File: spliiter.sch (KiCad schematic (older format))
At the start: 74 parts, among them U1 NE5532, U2 NE5532, U3 NE5532, U4 NE5532, U5 NE5532

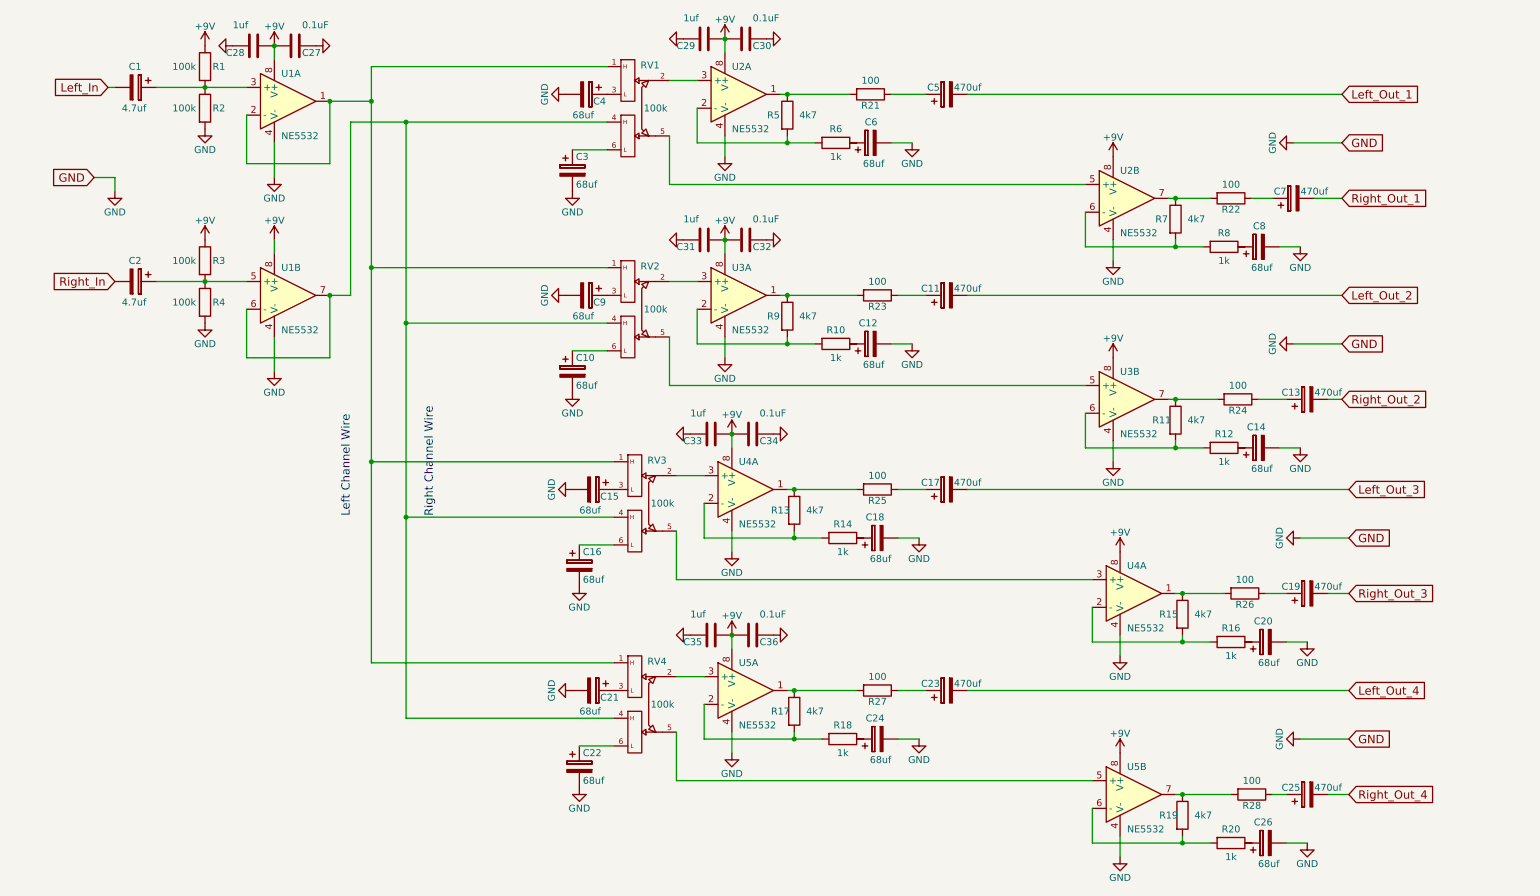
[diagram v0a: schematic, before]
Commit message: Replace +9V to VCC. Electrical rules checker passed
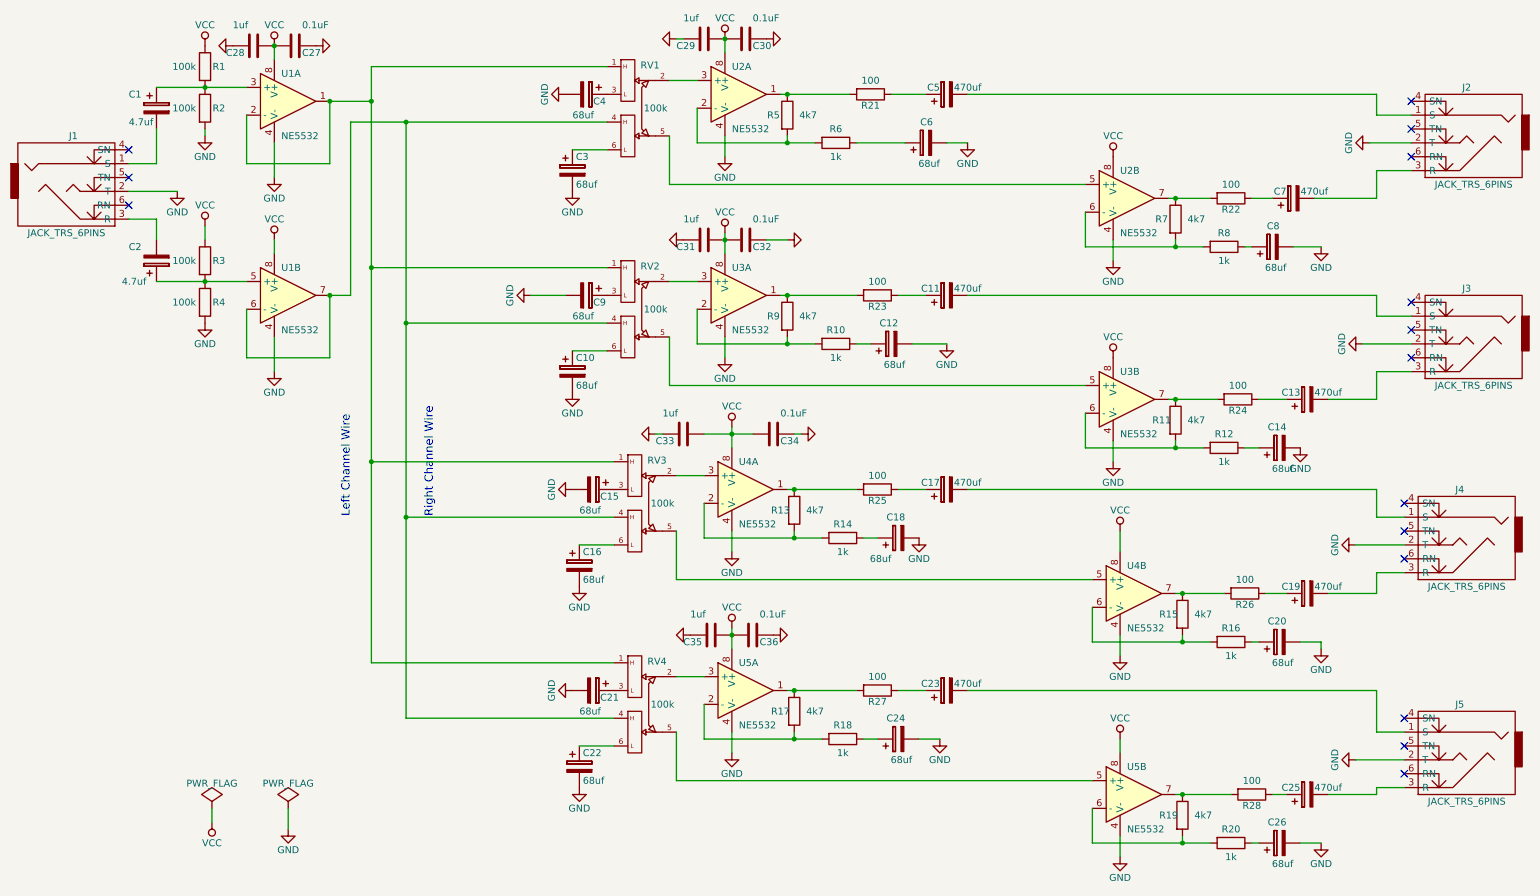
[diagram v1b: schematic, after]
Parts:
- removed U4: NE5532, symbol NE5532
- added J1, J2, J3, J4, J5: JACK_TRS_6PINS, symbol JACK_TRS_6PINS
- added unit 2 of U4
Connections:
- net GND: now also J1.2 (T), J2.2 (T), J3.2 (T), J4.2 (T), J5.2 (T), U4.4 (V-)
- net at R6.1: now also C6.1
- net at R8.1: now also C8.1
- net at R10.1: now also C12.1
- net at R12.1: now also C14.1
- net at RV3.5: now also U4.5 (+)
- net at R14.1: now also C18.1
- net at R15.1, R26.2: now also U4.7
- net at R15.2, R16.2: now also U4.6 (-)
- net at R16.1: now also C20.1
- net at R18.1: now also C24.1
- net at R20.1: now also C26.1
- net +9V renamed VCC
- net VCC: now also U4.8 (V+)
- net Left_In: no longer names the net of C1.2
- net Left_In: now also J1.1 (S)
- net Left_Out_1: no longer names the net of C5.2
- net Left_Out_1: now also J2.1 (S)
- net Left_Out_2: no longer names the net of C11.2
- net Left_Out_2: now also J3.1 (S)
- net Left_Out_3: no longer names the net of C17.2
- net Left_Out_3: now also J4.1 (S)
- net Left_Out_4: no longer names the net of C23.2
- net Left_Out_4: now also J5.1 (S)
- net Right_In: no longer names the net of C2.2
- net Right_In: now also J1.3 (R)
- net Right_Out_1: no longer names the net of C7.2
- net Right_Out_1: now also J2.3 (R)
- net Right_Out_2: no longer names the net of C13.2
- net Right_Out_2: now also J3.3 (R)
- net Right_Out_3: no longer names the net of C19.2
- net Right_Out_3: now also J4.3 (R)
- net Right_Out_4: no longer names the net of C25.2
- net Right_Out_4: now also J5.3 (R)
- no-connect marks 0 -> 15
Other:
- moved on the sheet: C1, C12, C14, C18, C2, C20, C24, C26, C33, C34, C6, C8

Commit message: add some values to netlist
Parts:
- C27, C28, C29, C30, C31, C32, C33, C34, C35, C36: footprint (none) -> Capacitors_SMD:C_0805_HandSoldering
- J1, J2, J3, J4, J5, RV1: footprint (none) -> Connect:PINHEAD1-3
- R1, R10, R11, R12, R13, R14, R15, R16, R17, R18, R19, R2, R20, R21, R22, R23, R24, R25, R26, R27, R28, R3, R4, R5, R6, R7, R8, R9: footprint (none) -> Resistors_SMD:R_0805_HandSoldering
- RV2, RV3, RV4: footprint (none) -> Connect:PINHEAD1-2
- U1, U2, U3, U4, U5: footprint (none) -> Housings_SOIC:SOIC-8_3.9x4.9mm_Pitch1.27mm

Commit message: fix pinheaders
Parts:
- RV2, RV3, RV4: footprint Connect:PINHEAD1-2 -> Connect:PINHEAD1-3
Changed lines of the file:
@@
 F 0 "RV2" H 4710 3010 50  0000 C CNN
 F 1 "100k" H 4750 2700 50  0000 C CNN
-F 2 "Connect:PINHEAD1-2" H 4550 2700 50  0001 C CNN
+F 2 "Connect:PINHEAD1-3" H 4550 2700 50  0001 C CNN
 F 3 "" H 4550 2700 50  0000 C CNN
 	1    4550 2700
@@
 F 0 "RV3" H 4760 4410 50  0000 C CNN
 F 1 "100k" H 4800 4100 50  0000 C CNN
-F 2 "Connect:PINHEAD1-2" H 4600 4100 50  0001 C CNN
+F 2 "Connect:PINHEAD1-3" H 4600 4100 50  0001 C CNN
 F 3 "" H 4600 4100 50  0000 C CNN
 	1    4600 4100
@@
 F 0 "RV4" H 4760 5860 50  0000 C CNN
 F 1 "100k" H 4800 5550 50  0000 C CNN
-F 2 "Connect:PINHEAD1-2" H 4600 5550 50  0001 C CNN
+F 2 "Connect:PINHEAD1-3" H 4600 5550 50  0001 C CNN
 F 3 "" H 4600 5550 50  0000 C CNN
 	1    4600 5550

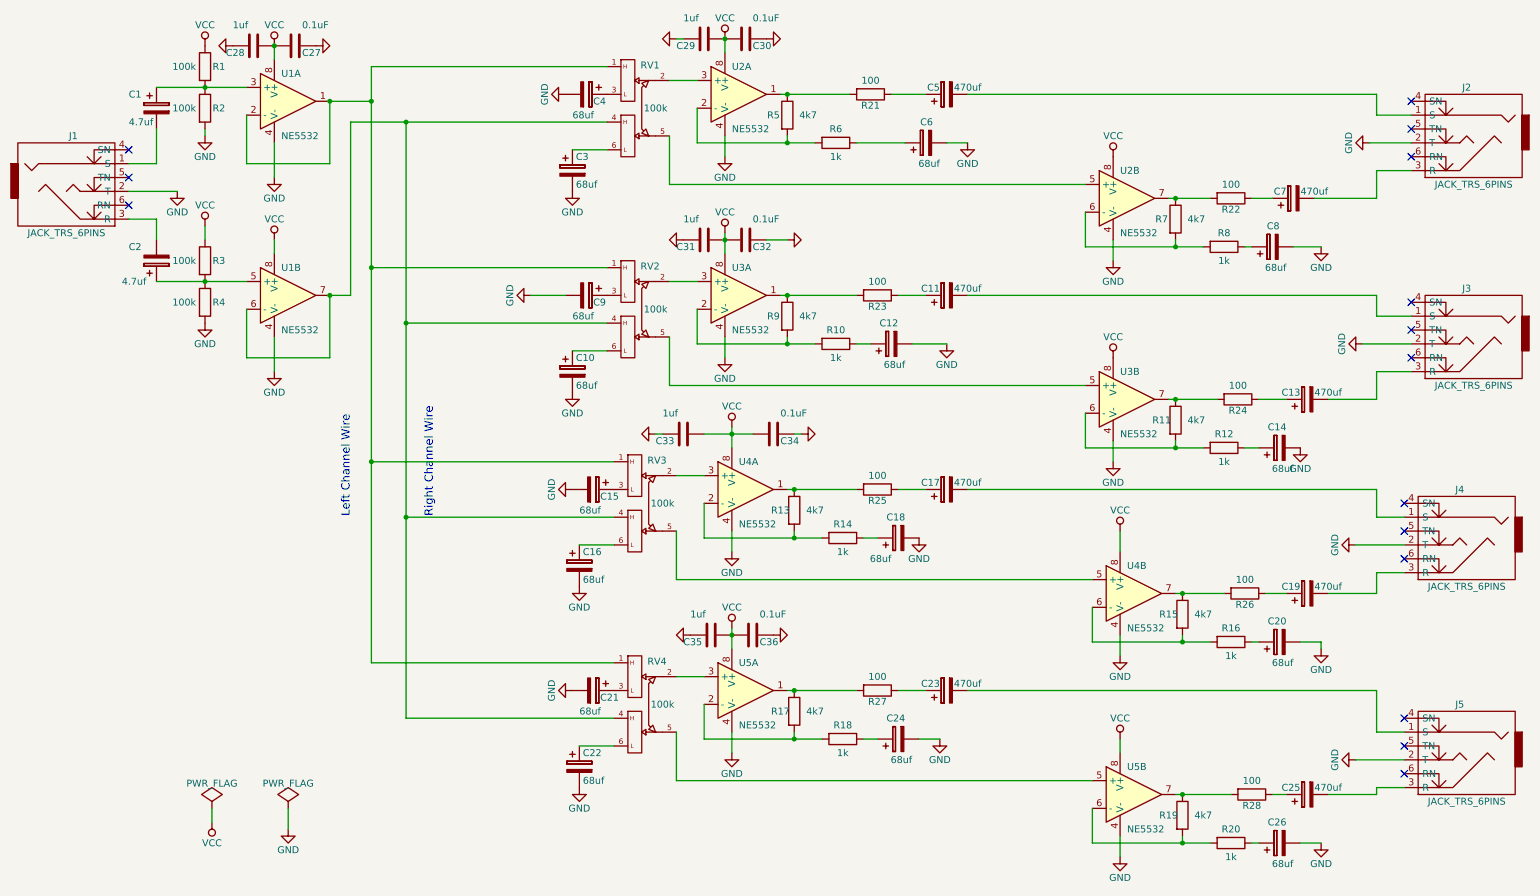
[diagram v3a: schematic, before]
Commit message: Component footprints assigned
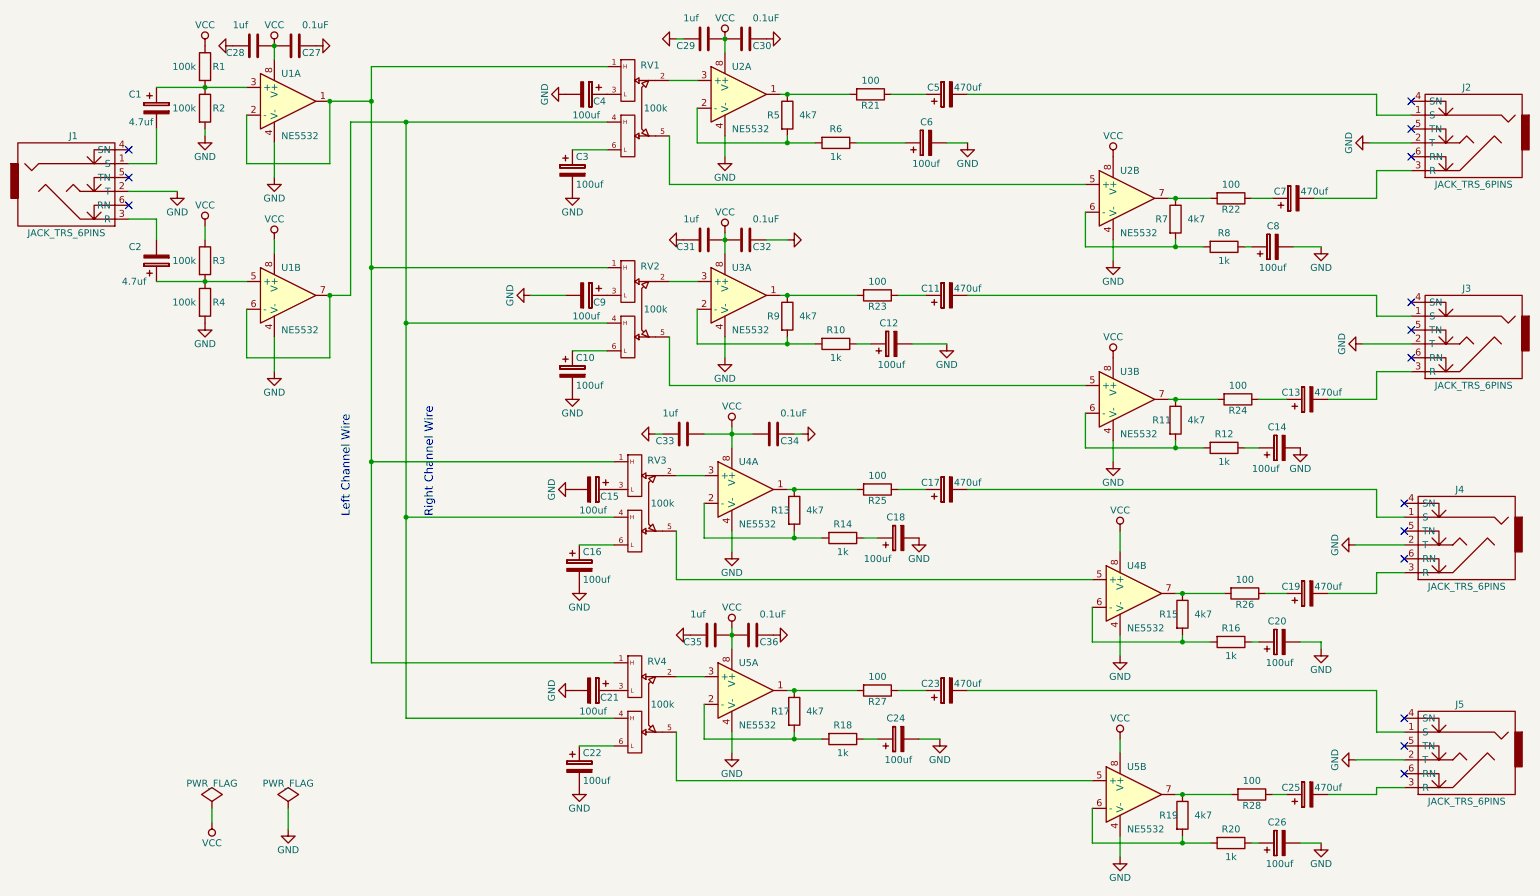
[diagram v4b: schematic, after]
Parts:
- C1, C2: footprint (none) -> Capacitors_SMD:c_elec_4x5.3
- C10, C12, C14, C15, C16, C18, C20, C21, C22, C24, C26, C3, C4, C6, C8, C9: value 68uf -> 100uf; footprint (none) -> Capacitors_SMD:c_elec_6.3x7.7
- C11, C13, C17, C19, C23, C25, C5, C7: footprint (none) -> Capacitors_SMD:c_elec_10x10.5
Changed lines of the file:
@@
 F 0 "C1" H 950 1350 50  0000 L CNN
 F 1 "4.7uf" H 950 1150 50  0000 L CNN
-F 2 "" H 1188 1100 50  0001 C CNN
+F 2 "Capacitors_SMD:c_elec_4x5.3" H 1188 1100 50  0001 C CNN
 F 3 "" H 1150 1250 50  0000 C CNN
 	1    1150 1250
@@
 F 0 "C2" H 950 2250 50  0000 L CNN
 F 1 "4.7uf" H 900 2500 50  0000 L CNN
-F 2 "" H 1188 2200 50  0001 C CNN
+F 2 "Capacitors_SMD:c_elec_4x5.3" H 1188 2200 50  0001 C CNN
 F 3 "" H 1150 2350 50  0000 C CNN
 	1    1150 2350
@@
 P 4250 1150
 F 0 "C4" V 4300 1200 50  0000 L CNN
-F 1 "68uf" V 4400 1050 50  0000 L CNN
-F 2 "" H 4288 1000 50  0001 C CNN
+F 1 "100uf" V 4400 1050 50  0000 L CNN
+F 2 "Capacitors_SMD:c_elec_6.3x7.7" H 4288 1000 50  0001 C CNN
 F 3 "" H 4250 1150 50  0000 C CNN
 	1    4250 1150
@@
 P 4150 1700
 F 0 "C3" H 4175 1800 50  0000 L CNN
-F 1 "68uf" H 4175 1600 50  0000 L CNN
-F 2 "" H 4188 1550 50  0001 C CNN
+F 1 "100uf" H 4175 1600 50  0000 L CNN
+F 2 "Capacitors_SMD:c_elec_6.3x7.7" H 4188 1550 50  0001 C CNN
 F 3 "" H 4150 1700 50  0000 C CNN
 	1    4150 1700
@@
 P 6700 1500
 F 0 "C6" V 6850 1450 50  0000 L CNN
-F 1 "68uf" V 6550 1400 50  0000 L CNN
-F 2 "" H 6738 1350 50  0001 C CNN
+F 1 "100uf" V 6550 1400 50  0000 L CNN
+F 2 "Capacitors_SMD:c_elec_6.3x7.7" H 6738 1350 50  0001 C CNN
 F 3 "" H 6700 1500 50  0000 C CNN
 	1    6700 1500
@@
 F 0 "C5" V 6900 1200 50  0000 L CNN
 F 1 "470uf" V 6900 900 50  0000 L CNN
-F 2 "" H 6888 1000 50  0001 C CNN
+F 2 "Capacitors_SMD:c_elec_10x10.5" H 6888 1000 50  0001 C CNN
 F 3 "" H 6850 1150 50  0000 C CNN
 	1    6850 1150
@@
 P 9200 2250
 F 0 "C8" V 9350 2200 50  0000 L CNN
-F 1 "68uf" V 9050 2150 50  0000 L CNN
-F 2 "" H 9238 2100 50  0001 C CNN
+F 1 "100uf" V 9050 2150 50  0000 L CNN
+F 2 "Capacitors_SMD:c_elec_6.3x7.7" H 9238 2100 50  0001 C CNN
 F 3 "" H 9200 2250 50  0000 C CNN
 	1    9200 2250
@@
 F 0 "C7" V 9400 1950 50  0000 L CNN
 F 1 "470uf" V 9400 1650 50  0000 L CNN
-F 2 "" H 9388 1750 50  0001 C CNN
+F 2 "Capacitors_SMD:c_elec_10x10.5" H 9388 1750 50  0001 C CNN
 F 3 "" H 9350 1900 50  0000 C CNN
 	1    9350 1900
@@
 P 4250 2600
 F 0 "C9" V 4300 2650 50  0000 L CNN
-F 1 "68uf" V 4400 2500 50  0000 L CNN
-F 2 "" H 4288 2450 50  0001 C CNN
+F 1 "100uf" V 4400 2500 50  0000 L CNN
+F 2 "Capacitors_SMD:c_elec_6.3x7.7" H 4288 2450 50  0001 C CNN
 F 3 "" H 4250 2600 50  0000 C CNN
 	1    4250 2600
@@
 P 4150 3150
 F 0 "C10" H 4175 3250 50  0000 L CNN
-F 1 "68uf" H 4175 3050 50  0000 L CNN
-F 2 "" H 4188 3000 50  0001 C CNN
+F 1 "100uf" H 4175 3050 50  0000 L CNN
+F 2 "Capacitors_SMD:c_elec_6.3x7.7" H 4188 3000 50  0001 C CNN
 F 3 "" H 4150 3150 50  0000 C CNN
 	1    4150 3150
@@
 P 6450 2950
 F 0 "C12" V 6600 2900 50  0000 L CNN
-F 1 "68uf" V 6300 2850 50  0000 L CNN
-F 2 "" H 6488 2800 50  0001 C CNN
+F 1 "100uf" V 6300 2850 50  0000 L CNN
+F 2 "Capacitors_SMD:c_elec_6.3x7.7" H 6488 2800 50  0001 C CNN
 F 3 "" H 6450 2950 50  0000 C CNN
 	1    6450 2950
@@
 F 0 "C11" V 6900 2650 50  0000 L CNN
 F 1 "470uf" V 6900 2350 50  0000 L CNN
-F 2 "" H 6888 2450 50  0001 C CNN
+F 2 "Capacitors_SMD:c_elec_10x10.5" H 6888 2450 50  0001 C CNN
 F 3 "" H 6850 2600 50  0000 C CNN
 	1    6850 2600
@@
 P 9250 3700
 F 0 "C14" V 9400 3650 50  0000 L CNN
-F 1 "68uf" V 9100 3600 50  0000 L CNN
-F 2 "" H 9288 3550 50  0001 C CNN
+F 1 "100uf" V 9100 3700 50  0000 L CNN
+F 2 "Capacitors_SMD:c_elec_6.3x7.7" H 9288 3550 50  0001 C CNN
 F 3 "" H 9250 3700 50  0000 C CNN
 	1    9250 3700
@@
 F 0 "C13" V 9500 3400 50  0000 L CNN
 F 1 "470uf" V 9500 3100 50  0000 L CNN
-F 2 "" H 9488 3200 50  0001 C CNN
+F 2 "Capacitors_SMD:c_elec_10x10.5" H 9488 3200 50  0001 C CNN
 F 3 "" H 9450 3350 50  0000 C CNN
 	1    9450 3350
@@
 P 4300 4000
 F 0 "C15" V 4350 4050 50  0000 L CNN
-F 1 "68uf" V 4450 3900 50  0000 L CNN
-F 2 "" H 4338 3850 50  0001 C CNN
+F 1 "100uf" V 4450 3900 50  0000 L CNN
+F 2 "Capacitors_SMD:c_elec_6.3x7.7" H 4338 3850 50  0001 C CNN
 F 3 "" H 4300 4000 50  0000 C CNN
 	1    4300 4000
@@
 P 4200 4550
 F 0 "C16" H 4225 4650 50  0000 L CNN
-F 1 "68uf" H 4225 4450 50  0000 L CNN
-F 2 "" H 4238 4400 50  0001 C CNN
+F 1 "100uf" H 4225 4450 50  0000 L CNN
+F 2 "Capacitors_SMD:c_elec_6.3x7.7" H 4238 4400 50  0001 C CNN
 F 3 "" H 4200 4550 50  0000 C CNN
 	1    4200 4550
@@
 P 6500 4350
 F 0 "C18" V 6650 4300 50  0000 L CNN
-F 1 "68uf" V 6350 4400 50  0000 L CNN
-F 2 "" H 6538 4200 50  0001 C CNN
+F 1 "100uf" V 6350 4400 50  0000 L CNN
+F 2 "Capacitors_SMD:c_elec_6.3x7.7" H 6538 4200 50  0001 C CNN
 F 3 "" H 6500 4350 50  0000 C CNN
 	1    6500 4350
@@
 F 0 "C17" V 6900 4050 50  0000 L CNN
 F 1 "470uf" V 6900 3750 50  0000 L CNN
-F 2 "" H 6888 3850 50  0001 C CNN
+F 2 "Capacitors_SMD:c_elec_10x10.5" H 6888 3850 50  0001 C CNN
 F 3 "" H 6850 4000 50  0000 C CNN
 	1    6850 4000
@@
 P 9250 5100
 F 0 "C20" V 9400 5050 50  0000 L CNN
-F 1 "68uf" V 9100 5000 50  0000 L CNN
-F 2 "" H 9288 4950 50  0001 C CNN
+F 1 "100uf" V 9100 5000 50  0000 L CNN
+F 2 "Capacitors_SMD:c_elec_6.3x7.7" H 9288 4950 50  0001 C CNN
 F 3 "" H 9250 5100 50  0000 C CNN
 	1    9250 5100
@@
 F 0 "C19" V 9500 4800 50  0000 L CNN
 F 1 "470uf" V 9500 4500 50  0000 L CNN
-F 2 "" H 9488 4600 50  0001 C CNN
+F 2 "Capacitors_SMD:c_elec_10x10.5" H 9488 4600 50  0001 C CNN
 F 3 "" H 9450 4750 50  0000 C CNN
 	1    9450 4750
@@
 P 4300 5450
 F 0 "C21" V 4350 5500 50  0000 L CNN
-F 1 "68uf" V 4450 5350 50  0000 L CNN
-F 2 "" H 4338 5300 50  0001 C CNN
+F 1 "100uf" V 4450 5350 50  0000 L CNN
+F 2 "Capacitors_SMD:c_elec_6.3x7.7" H 4338 5300 50  0001 C CNN
 F 3 "" H 4300 5450 50  0000 C CNN
 	1    4300 5450
@@
 P 4200 6000
 F 0 "C22" H 4225 6100 50  0000 L CNN
-F 1 "68uf" H 4225 5900 50  0000 L CNN
-F 2 "" H 4238 5850 50  0001 C CNN
+F 1 "100uf" H 4225 5900 50  0000 L CNN
+F 2 "Capacitors_SMD:c_elec_6.3x7.7" H 4238 5850 50  0001 C CNN
 F 3 "" H 4200 6000 50  0000 C CNN
 	1    4200 6000
@@
 P 6500 5800
 F 0 "C24" V 6650 5750 50  0000 L CNN
-F 1 "68uf" V 6350 5700 50  0000 L CNN
-F 2 "" H 6538 5650 50  0001 C CNN
+F 1 "100uf" V 6350 5700 50  0000 L CNN
+F 2 "Capacitors_SMD:c_elec_6.3x7.7" H 6538 5650 50  0001 C CNN
 F 3 "" H 6500 5800 50  0000 C CNN
 	1    6500 5800
@@
 F 0 "C23" V 6900 5500 50  0000 L CNN
 F 1 "470uf" V 6900 5200 50  0000 L CNN
-F 2 "" H 6888 5300 50  0001 C CNN
+F 2 "Capacitors_SMD:c_elec_10x10.5" H 6888 5300 50  0001 C CNN
 F 3 "" H 6850 5450 50  0000 C CNN
 	1    6850 5450
@@
 P 9250 6550
 F 0 "C26" V 9400 6500 50  0000 L CNN
-F 1 "68uf" V 9100 6450 50  0000 L CNN
-F 2 "" H 9288 6400 50  0001 C CNN
+F 1 "100uf" V 9100 6450 50  0000 L CNN
+F 2 "Capacitors_SMD:c_elec_6.3x7.7" H 9288 6400 50  0001 C CNN
 F 3 "" H 9250 6550 50  0000 C CNN
 	1    9250 6550
@@
 F 0 "C25" V 9500 6250 50  0000 L CNN
 F 1 "470uf" V 9500 5950 50  0000 L CNN
-F 2 "" H 9488 6050 50  0001 C CNN
+F 2 "Capacitors_SMD:c_elec_10x10.5" H 9488 6050 50  0001 C CNN
 F 3 "" H 9450 6200 50  0000 C CNN
 	1    9450 6200

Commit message: pcb done
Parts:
- RV1, RV2, RV3, RV4: footprint Connect:PINHEAD1-3 -> Connect:PINHEAD1-6
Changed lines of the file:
@@
 F 0 "RV1" H 4710 1560 50  0000 C CNN
 F 1 "100k" H 4750 1250 50  0000 C CNN
-F 2 "Connect:PINHEAD1-3" H 4550 1250 50  0001 C CNN
+F 2 "Connect:PINHEAD1-6" H 4550 1250 50  0001 C CNN
 F 3 "" H 4550 1250 50  0000 C CNN
 	1    4550 1250
@@
 F 0 "RV2" H 4710 3010 50  0000 C CNN
 F 1 "100k" H 4750 2700 50  0000 C CNN
-F 2 "Connect:PINHEAD1-3" H 4550 2700 50  0001 C CNN
+F 2 "Connect:PINHEAD1-6" H 4550 2700 50  0001 C CNN
 F 3 "" H 4550 2700 50  0000 C CNN
 	1    4550 2700
@@
 F 0 "RV3" H 4760 4410 50  0000 C CNN
 F 1 "100k" H 4800 4100 50  0000 C CNN
-F 2 "Connect:PINHEAD1-3" H 4600 4100 50  0001 C CNN
+F 2 "Connect:PINHEAD1-6" H 4600 4100 50  0001 C CNN
 F 3 "" H 4600 4100 50  0000 C CNN
 	1    4600 4100
@@
 F 0 "RV4" H 4760 5860 50  0000 C CNN
 F 1 "100k" H 4800 5550 50  0000 C CNN
-F 2 "Connect:PINHEAD1-3" H 4600 5550 50  0001 C CNN
+F 2 "Connect:PINHEAD1-6" H 4600 5550 50  0001 C CNN
 F 3 "" H 4600 5550 50  0000 C CNN
 	1    4600 5550
